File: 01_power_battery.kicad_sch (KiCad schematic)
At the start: 210 parts, among them Q13 CSD19537Q3 100V AUX reverse F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, Q14 BSS138 fast reverse-gate pull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, Q21 SiSS4409DN 40V reverse-blocki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, Q22 SiSS4409DN 40V reverse-blocki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, Q23 SiSS4409DN 40V reverse-blocki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, Q24 SiSS4409DN 40V reverse-blocki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, Q25 CSD17575Q3 battery power-path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, Q26 SiSS4409DN 40V reverse-blocki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, Q2600 CSD17577Q3A 30V switching FET, Q2601 CSD17577Q3A 30V switching FET, Q2602 CSD17577Q3A 30V switching FET, Q2603 CSD17577Q3A 30V switching FET, Q2604 BSS138, Q2605 BSS138, Q2620 CSD19537Q3 100V, Q2621 CSD19537Q3 100V, Q2622 CSD19537Q3 100V, Q2623 CSD19537Q3 100V, Q2644 BSS138 AUX discharge, Q2650 CSD19537Q3 100V, Q2660 CSD18540Q5B AON pass FET, Q27 SiSS4409DN 40V reverse-blocki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, Q28 SiSS4409DN 40V reverse-blocki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, Q29 SiSS4409DN 40V reverse-blocki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, Q700 BSS138, Q702 BSS138, U10 BQ34Z100-G1 protected-pack ga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, U12 TPS26630RGER 3A AUX eFuse / s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, U15 LTC4418IUF#PBF dual-input sel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, U16 LTC4418IUF#PBF dual-input sel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, U2 ISL9241IRTZ, U2620 LM74700QDBVRQ1, U2621 LM74700QDBVRQ1, U2634 TPS3700DDCR charger-bias dete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, U2635 TCA9537DGSR power status and 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, U2644 SN74LVC1G04DBVR AUX discharge, U2650 LM74700QDBVRQ1 system standby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, U2660 LTC4231IMS-1#PBF standby curr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, U718 LTC4368IMS-2#PBF standby brea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

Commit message: tidy up the input and standby power
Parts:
- added C2686: 100n 50V U16 V1 local, Capacitor_SMD:C_0603_1608Metric, symbol Device:C
- added C2687: 100n 50V U16 VS1 local, Capacitor_SMD:C_0603_1608Metric, symbol Device:C
- added C2688: 100n 50V U15 VOUT local, Capacitor_SMD:C_0603_1608Metric, symbol Device:C
- C747: value 100n 50V stage2 VS1 local -> 100n 50V U15 VS2 local
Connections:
- net GND: now also C2686.2, C2687.2, C2688.2
- net PD2_VBUS_GATED: now also C2686.1
- net ST2_USB_FET_COMMON: now also C2687.1
- net VBUS_COMBINED: now also C2688.1
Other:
- note added: "CHG_ENABLE releases the NTC inhibit after qualified pack checks. The fixed 10k state is not a cell-temperature measurement."
- note added: "Pack protection is on the BMS. J2071 receives PACK_POS_FUSED and FG_VSS; return current reaches GND through RS1."
- note removed: "The charger NTC pin receives a hardware inhibit from the BMS permit. The fixed 10k state is not a cell-temperature measurement."
- note removed: "U11 accepts about 8.45-13.57V nominal; 11mOhm RS10 gives 4.55A nominal and <=5.51A worst-case trips."
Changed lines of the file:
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@@
   (effects (font (size 1.27 1.27)) (justify left bottom))
-)
-(symbol
-  (lib_id "Device:C")
-  (at 635 293.37 0)
-  (unit 1)
-  (exclude_from_sim no)
-  (in_bom yes)
-  (on_board yes)
-  (dnp no)
-  (property "Reference" "C747" (at 635 290.83 0) (effects (font (size 1.27 1.27))))
-  (property "Value" "100n 50V stage2 VS1 local" (at 635 295.91 0) (effects (font (size 1.27 1.27))))
-  (property "Footprint" "Capacitor_SMD:C_0603_1608Metric" (at 635 293.37 0) (effects (font (size 1.27 1.27)) (hide yes)))
-  (property "Datasheet" "" (at 635 293.37 0) (effects (font (size 1.27 1.27)) (hide yes)))
-  (property "Manufacturer" "Murata" (at 635 293.37 0) (effects (font (size 1.27 1.27)) (hide yes)))
-  (property "MPN" "GRM188R71H104KA93D" (at 635 293.37 0) (effects (font (size 1.27 1.27)) (hide yes)))
-  (pin "1")
-  (pin "2")
-  (instances
-    (project "ducktop2"
-      (path "/577b7ab7-60d3-5949-82f8-bb269dce837a"
-        (reference "C747")
-        (unit 1)
-      )
-    )
-  )
 )
 (label "ST2_MAIN_FET_COMMON"
@@
 (text "RS2600 is the 20mOhm input shunt. RS2601 is the separate 10mOhm battery-current shunt; both need Kelvin routing." (at 20.32 294.64 0) (effects (font (size 1.27 1.27)) (justify left)))
 (text "Q25 is the ISL9241 battery-path FET. Battery standby comes through VSYS and the discharge shunt; disabling Mu keeps button wake available." (at 20.32 302.26 0) (effects (font (size 1.27 1.27)) (justify left)))
-(text "U11 accepts about 8.45-13.57V nominal; 11mOhm RS10 gives 4.55A nominal and <=5.51A worst-case trips." (at 20.32 309.88 0) (effects (font (size 1.27 1.27)) (justify left)))
-(text "The charger NTC pin receives a hardware inhibit from the BMS permit. The fixed 10k state is not a cell-temperature measurement." (at 20.32 317.5 0) (effects (font (size 1.27 1.27)) (justify left)))
 (text "STARTUP: keep Mu enable low and PROCHOT asserted. Read TCPC PD Status 0x40 and active PDO/RDO 0x34/0x35 before selecting a source." (at 20.32 325.12 0) (effects (font (size 1.27 1.27)) (justify left)))
 (text "Require the qualified VSYS threshold before Mu enable and confirm MU_12V_PG. Source, charger, watchdog or PG faults revoke enable; profile gates remain off until qualified." (at 20.32 332.74 0) (effects (font (size 1.27 1.27)) (justify left)))
@@
 )
   (embedded_fonts no)
-)
+(symbol
+  (lib_id "Device:C")
+  (at 635 293.37 0)
+  (unit 1)
+  (exclude_from_sim no)
+  (in_bom yes)
+  (on_board yes)
+  (dnp no)
+  (property "Reference" "C747" (at 635 290.83 0) (effects (font (size 1.27 1.27))))
+  (property "Value" "100n 50V U15 VS2 local" (at 635 295.91 0) (effects (font (size 1.27 1.27))))
+  (property "Footprint" "Capacitor_SMD:C_0603_1608Metric" (at 635 293.37 0) (effects (font (size 1.27 1.27)) (hide yes)))
+  (property "Datasheet" "" (at 635 293.37 0) (effects (font (size 1.27 1.27)) (hide yes)))
+  (property "Manufacturer" "Murata" (at 635 293.37 0) (effects (font (size 1.27 1.27)) (hide yes)))
+  (property "MPN" "GRM188R71H104KA93D" (at 635 293.37 0) (effects (font (size 1.27 1.27)) (hide yes)))
+  (pin "1")
+  (pin "2")
+  (instances
+    (project "ducktop2"
+      (path "/577b7ab7-60d3-5949-82f8-bb269dce837a"
+        (reference "C747")
+        (unit 1)
+      )
+    )
+  )
+)
+(symbol
+  (lib_id "Device:C")
+  (at 635 519.43 0)
+  (unit 1)
+  (exclude_from_sim no)
+  (in_bom yes)
+  (on_board yes)
+  (dnp no)
+  (property "Reference" "C2686" (at 640.08 518.16 0) (effects (font (size 1.27 1.27)) (justify left)))
+  (property "Value" "100n 50V U16 V1 local" (at 640.08 520.7 0) (effects (font (size 1.27 1.27)) (justify left)))
+  (property "Footprint" "Capacitor_SMD:C_0603_1608Metric" (at 635 519.43 0) (effects (font (size 1.27 1.27)) (hide yes)))
+  (property "Datasheet" "" (at 635 519.43 0) (effects (font (size 1.27 1.27)) (hide yes)))
+  (property "Manufacturer" "Murata" (at 635 519.43 0) (effects (font (size 1.27 1.27)) (hide yes)))
+  (property "MPN" "GRM188R71H104KA93D" (at 635 519.43 0) (effects (font (size 1.27 1.27)) (hide yes)))
+  (property "DecouplingFor" "U16 V1" (at 635 519.43 0) (effects (font (size 1.27 1.27)) (hide yes)))
+  (pin "1")
+  (pin "2")
+  (instances
+    (project "ducktop2"
+      (path "/577b7ab7-60d3-5949-82f8-bb269dce837a"
+        (reference "C2686")
+        (unit 1)
+      )
+    )
+  )
+)
+(hierarchical_label "PD2_VBUS_GATED"
+  (shape bidirectional)
+  (at 635 515.62 0)
+  (effects (font (size 1.27 1.27)) (justify left bottom))
+)
+(label "GND"
+  (at 635 523.24 0)
+  (effects (font (size 1.27 1.27)) (justify left bottom))
+)
+(symbol
+  (lib_id "Device:C")
+  (at 709.93 519.43 0)
+  (unit 1)
+  (exclude_from_sim no)
+  (in_bom yes)
+  (on_board yes)
+  (dnp no)
+  (property "Reference" "C2687" (at 715.01 518.16 0) (effects (font (size 1.27 1.27)) (justify left)))
+  (property "Value" "100n 50V U16 VS1 local" (at 715.01 520.7 0) (effects (font (size 1.27 1.27)) (justify left)))
+  (property "Footprint" "Capacitor_SMD:C_0603_1608Metric" (at 709.93 519.43 0) (effects (font (size 1.27 1.27)) (hide yes)))
+  (property "Datasheet" "" (at 709.93 519.43 0) (effects (font (size 1.27 1.27)) (hide yes)))
+  (property "Manufacturer" "Murata" (at 709.93 519.43 0) (effects (font (size 1.27 1.27)) (hide yes)))
+  (property "MPN" "GRM188R71H104KA93D" (at 709.93 519.43 0) (effects (font (size 1.27 1.27)) (hide yes)))
+  (property "DecouplingFor" "U16 VS1" (at 709.93 519.43 0) (effects (font (size 1.27 1.27)) (hide yes)))
+  (pin "1")
+  (pin "2")
+  (instances
+    (project "ducktop2"
+      (path "/577b7ab7-60d3-5949-82f8-bb269dce837a"
+        (reference "C2687")
+        (unit 1)
+      )
+    )
+  )
+)
+(label "ST2_USB_FET_COMMON"
+  (at 709.93 515.62 0)
+  (effects (font (size 1.27 1.27)) (justify left bottom))
+)
+(label "GND"
+  (at 709.93 523.24 0)
+  (effects (font (size 1.27 1.27)) (justify left bottom))
+)
+(symbol
+  (lib_id "Device:C")
+  (at 685.8 293.37 0)
+  (unit 1)
+  (exclude_from_sim no)
+  (in_bom yes)
+  (on_board yes)
+  (dnp no)
+  (property "Reference" "C2688" (at 690.88 292.1 0) (effects (font (size 1.27 1.27)) (justify left)))
+  (property "Value" "100n 50V U15 VOUT local" (at 690.88 294.64 0) (effects (font (size 1.27 1.27)) (justify left)))
+  (property "Footprint" "Capacitor_SMD:C_0603_1608Metric" (at 685.8 293.37 0) (effects (font (size 1.27 1.27)) (hide yes)))
+  (property "Datasheet" "" (at 685.8 293.37 0) (effects (font (size 1.27 1.27)) (hide yes)))
+  (property "Manufacturer" "Murata" (at 685.8 293.37 0) (effects (font (size 1.27 1.27)) (hide yes)))
+  (property "MPN" "GRM188R71H104KA93D" (at 685.8 293.37 0) (effects (font (size 1.27 1.27)) (hide yes)))
+  (property "DecouplingFor" "U15 VOUT" (at 685.8 293.37 0) (effects (font (size 1.27 1.27)) (hide yes)))
+  (pin "1")
+  (pin "2")
+  (instances
+    (project "ducktop2"
+      (path "/577b7ab7-60d3-5949-82f8-bb269dce837a"
+        (reference "C2688")
+        (unit 1)
+      )
+    )
+  )
+)
+(label "VBUS_COMBINED"
+  (at 685.8 289.56 0)
+  (effects (font (size 1.27 1.27)) (justify left bottom))
+)
+(label "GND"
+  (at 685.8 297.18 0)
+  (effects (font (size 1.27 1.27)) (justify left bottom))
+)
+(text "Pack protection is on the BMS. J2071 receives PACK_POS_FUSED and FG_VSS; return current reaches GND through RS1." (at 20.32 309.88 0) (effects (font (size 1.27 1.27)) (justify left)))
+(text "CHG_ENABLE releases the NTC inhibit after qualified pack checks. The fixed 10k state is not a cell-temperature measurement." (at 20.32 317.5 0) (effects (font (size 1.27 1.27)) (justify left)))
+)

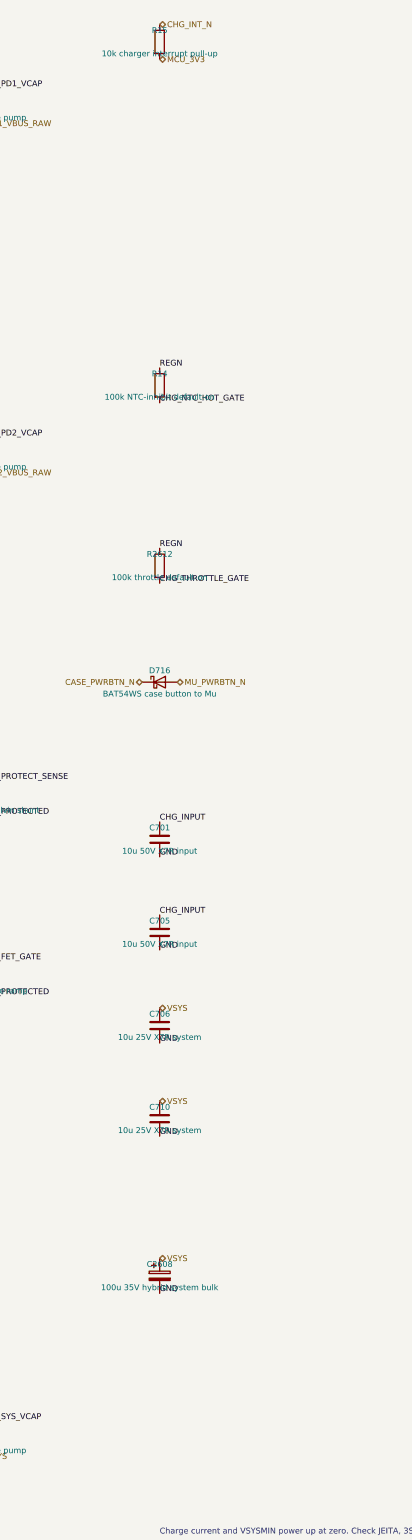
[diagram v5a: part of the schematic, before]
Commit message: sort out the main-board power placement and usb footprints
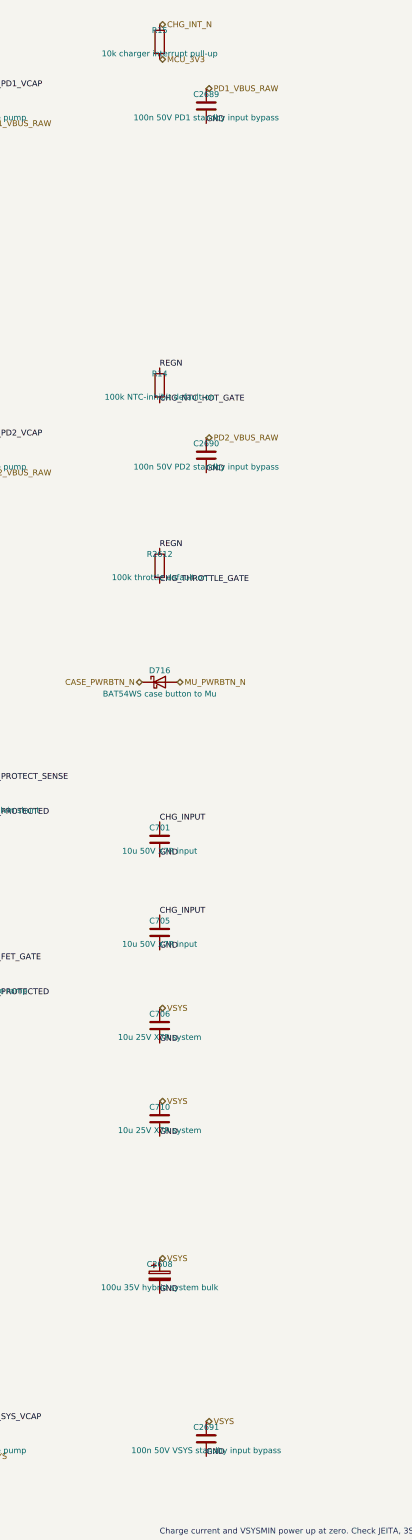
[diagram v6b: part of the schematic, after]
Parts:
- added C2689: 100n 50V PD1 standby input bypass, Capacitor_SMD:C_0603_1608Metric, symbol Device:C
- added C2690: 100n 50V PD2 standby input bypass, Capacitor_SMD:C_0603_1608Metric, symbol Device:C
- added C2691: 100n 50V VSYS standby input bypass, Capacitor_SMD:C_0603_1608Metric, symbol Device:C
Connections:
- net GND: now also C2689.2, C2690.2, C2691.2
- net PD1_VBUS_RAW: now also C2689.1
- net PD2_VBUS_RAW: now also C2690.1
- net VSYS: now also C2691.1
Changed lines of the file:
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@@
 (text "Pack protection is on the BMS. J2071 receives PACK_POS_FUSED and FG_VSS; return current reaches GND through RS1." (at 20.32 309.88 0) (effects (font (size 1.27 1.27)) (justify left)))
 (text "CHG_ENABLE releases the NTC inhibit after qualified pack checks. The fixed 10k state is not a cell-temperature measurement." (at 20.32 317.5 0) (effects (font (size 1.27 1.27)) (justify left)))
+(symbol
+  (lib_id "Device:C")
+  (at 859.79 439.42 0)
+  (unit 1)
+  (exclude_from_sim no)
+  (in_bom yes)
+  (on_board yes)
+  (dnp no)
+  (property "Reference" "C2689" (at 859.79 436.88 0) (effects (font (size 1.27 1.27))))
+  (property "Value" "100n 50V PD1 standby input bypass" (at 859.79 441.96 0) (effects (font (size 1.27 1.27))))
+  (property "Footprint" "Capacitor_SMD:C_0603_1608Metric" (at 859.79 439.42 0) (effects (font (size 1.27 1.27)) (hide yes)))
+  (property "Datasheet" "" (at 859.79 439.42 0) (effects (font (size 1.27 1.27)) (hide yes)))
+  (property "Manufacturer" "Murata" (at 859.79 439.42 0) (effects (font (size 1.27 1.27)) (hide yes)))
+  (property "MPN" "GRM188R71H104KA93D" (at 859.79 439.42 0) (effects (font (size 1.27 1.27)) (hide yes)))
+  (pin "1")
+  (pin "2")
+  (instances
+    (project "ducktop2"
+      (path "/577b7ab7-60d3-5949-82f8-bb269dce837a"
+        (reference "C2689")
+        (unit 1)
+      )
+    )
+  )
 )
+(hierarchical_label "PD1_VBUS_RAW"
+  (shape bidirectional)
+  (at 859.79 435.61 0)
+  (effects (font (size 1.27 1.27)) (justify left bottom))
+)
+(label "GND"
+  (at 859.79 443.23 0)
+  (effects (font (size 1.27 1.27)) (justify left bottom))
+)
+(symbol
+  (lib_id "Device:C")
+  (at 859.79 515.62 0)
+  (unit 1)
+  (exclude_from_sim no)
+  (in_bom yes)
+  (on_board yes)
+  (dnp no)
+  (property "Reference" "C2690" (at 859.79 513.08 0) (effects (font (size 1.27 1.27))))
+  (property "Value" "100n 50V PD2 standby input bypass" (at 859.79 518.16 0) (effects (font (size 1.27 1.27))))
+  (property "Footprint" "Capacitor_SMD:C_0603_1608Metric" (at 859.79 515.62 0) (effects (font (size 1.27 1.27)) (hide yes)))
+  (property "Datasheet" "" (at 859.79 515.62 0) (effects (font (size 1.27 1.27)) (hide yes)))
+  (property "Manufacturer" "Murata" (at 859.79 515.62 0) (effects (font (size 1.27 1.27)) (hide yes)))
+  (property "MPN" "GRM188R71H104KA93D" (at 859.79 515.62 0) (effects (font (size 1.27 1.27)) (hide yes)))
+  (pin "1")
+  (pin "2")
+  (instances
+    (project "ducktop2"
+      (path "/577b7ab7-60d3-5949-82f8-bb269dce837a"
+        (reference "C2690")
+        (unit 1)
+      )
+    )
+  )
+)
+(hierarchical_label "PD2_VBUS_RAW"
+  (shape bidirectional)
+  (at 859.79 511.81 0)
+  (effects (font (size 1.27 1.27)) (justify left bottom))
+)
+(label "GND"
+  (at 859.79 519.43 0)
+  (effects (font (size 1.27 1.27)) (justify left bottom))
+)
+(symbol
+  (lib_id "Device:C")
+  (at 859.79 730.25 0)
+  (unit 1)
+  (exclude_from_sim no)
+  (in_bom yes)
+  (on_board yes)
+  (dnp no)
+  (property "Reference" "C2691" (at 859.79 727.71 0) (effects (font (size 1.27 1.27))))
+  (property "Value" "100n 50V VSYS standby input bypass" (at 859.79 732.79 0) (effects (font (size 1.27 1.27))))
+  (property "Footprint" "Capacitor_SMD:C_0603_1608Metric" (at 859.79 730.25 0) (effects (font (size 1.27 1.27)) (hide yes)))
+  (property "Datasheet" "" (at 859.79 730.25 0) (effects (font (size 1.27 1.27)) (hide yes)))
+  (property "Manufacturer" "Murata" (at 859.79 730.25 0) (effects (font (size 1.27 1.27)) (hide yes)))
+  (property "MPN" "GRM188R71H104KA93D" (at 859.79 730.25 0) (effects (font (size 1.27 1.27)) (hide yes)))
+  (pin "1")
+  (pin "2")
+  (instances
+    (project "ducktop2"
+      (path "/577b7ab7-60d3-5949-82f8-bb269dce837a"
+        (reference "C2691")
+        (unit 1)
+      )
+    )
+  )
+)
+(hierarchical_label "VSYS"
+  (shape bidirectional)
+  (at 859.79 726.44 0)
+  (effects (font (size 1.27 1.27)) (justify left bottom))
+)
+(label "GND"
+  (at 859.79 734.06 0)
+  (effects (font (size 1.27 1.27)) (justify left bottom))
+)
+)
